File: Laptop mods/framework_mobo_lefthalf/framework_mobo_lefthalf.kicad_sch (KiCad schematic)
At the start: 48 parts, among them J1 USB_C_Receptacle, J2 IF, J5 Display, M1 AltmodeFriend, Q1 BC847, Q2 Q_PMOS_GSD, Q3 BC847, Q4 Q_PMOS_GSD, U1 VL170, U2 FSUSB30MUX, U3 AP1117-33

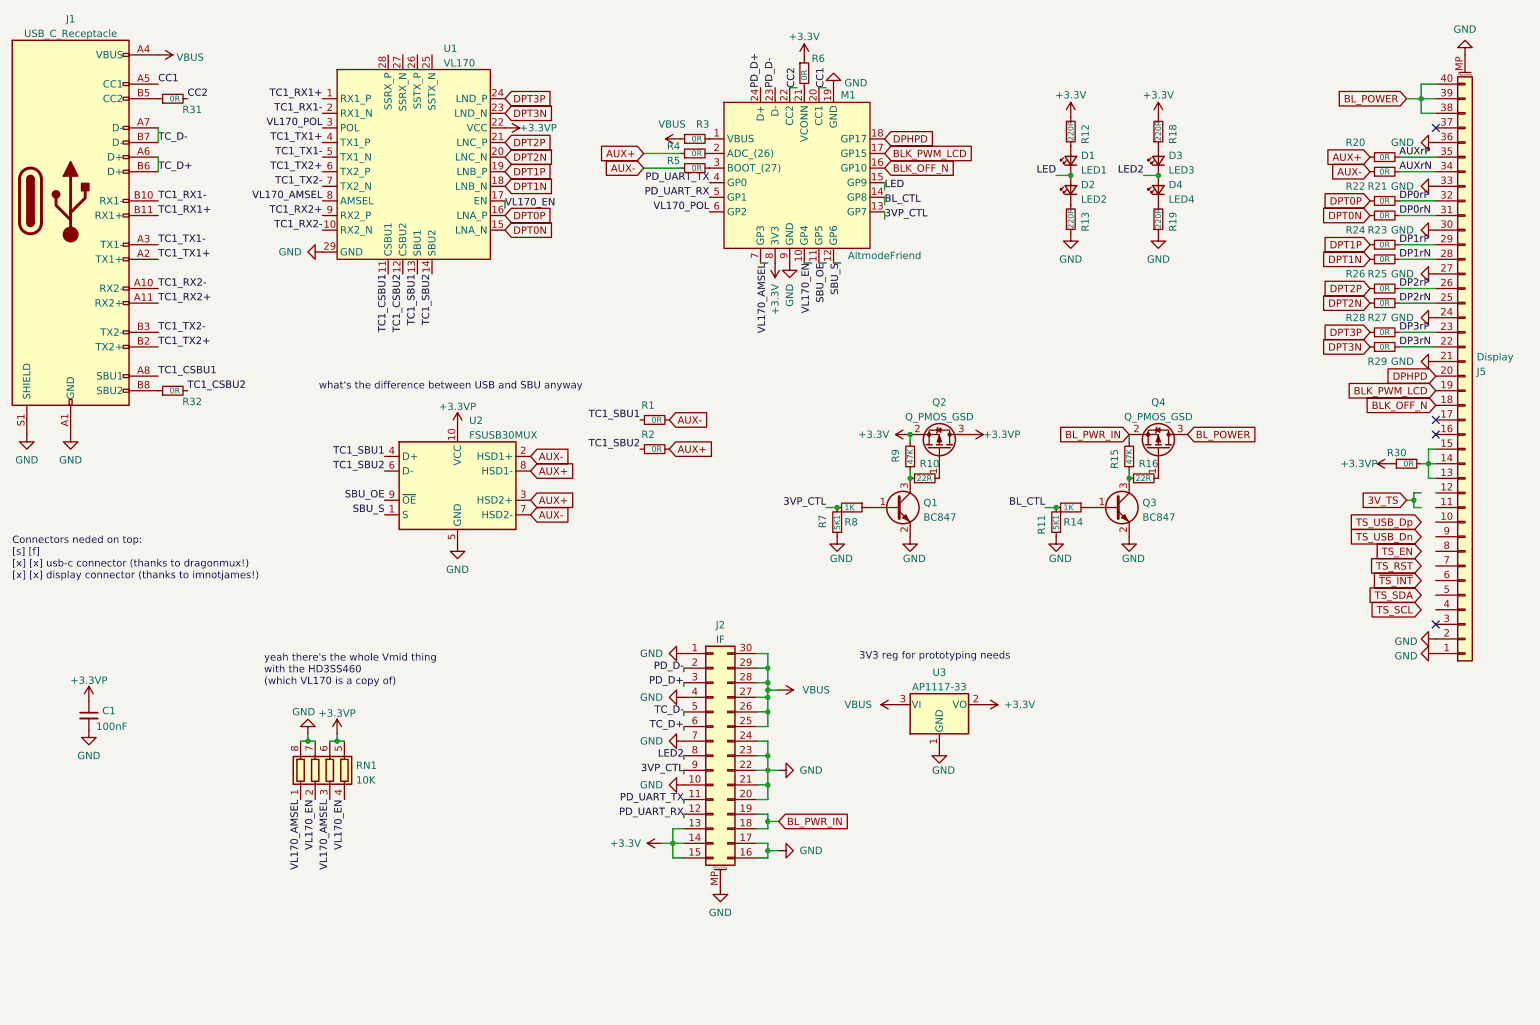
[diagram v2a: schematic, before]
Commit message: framework_mobo_lefthalf: had to rearrange order of DP lanes from the mux, now done
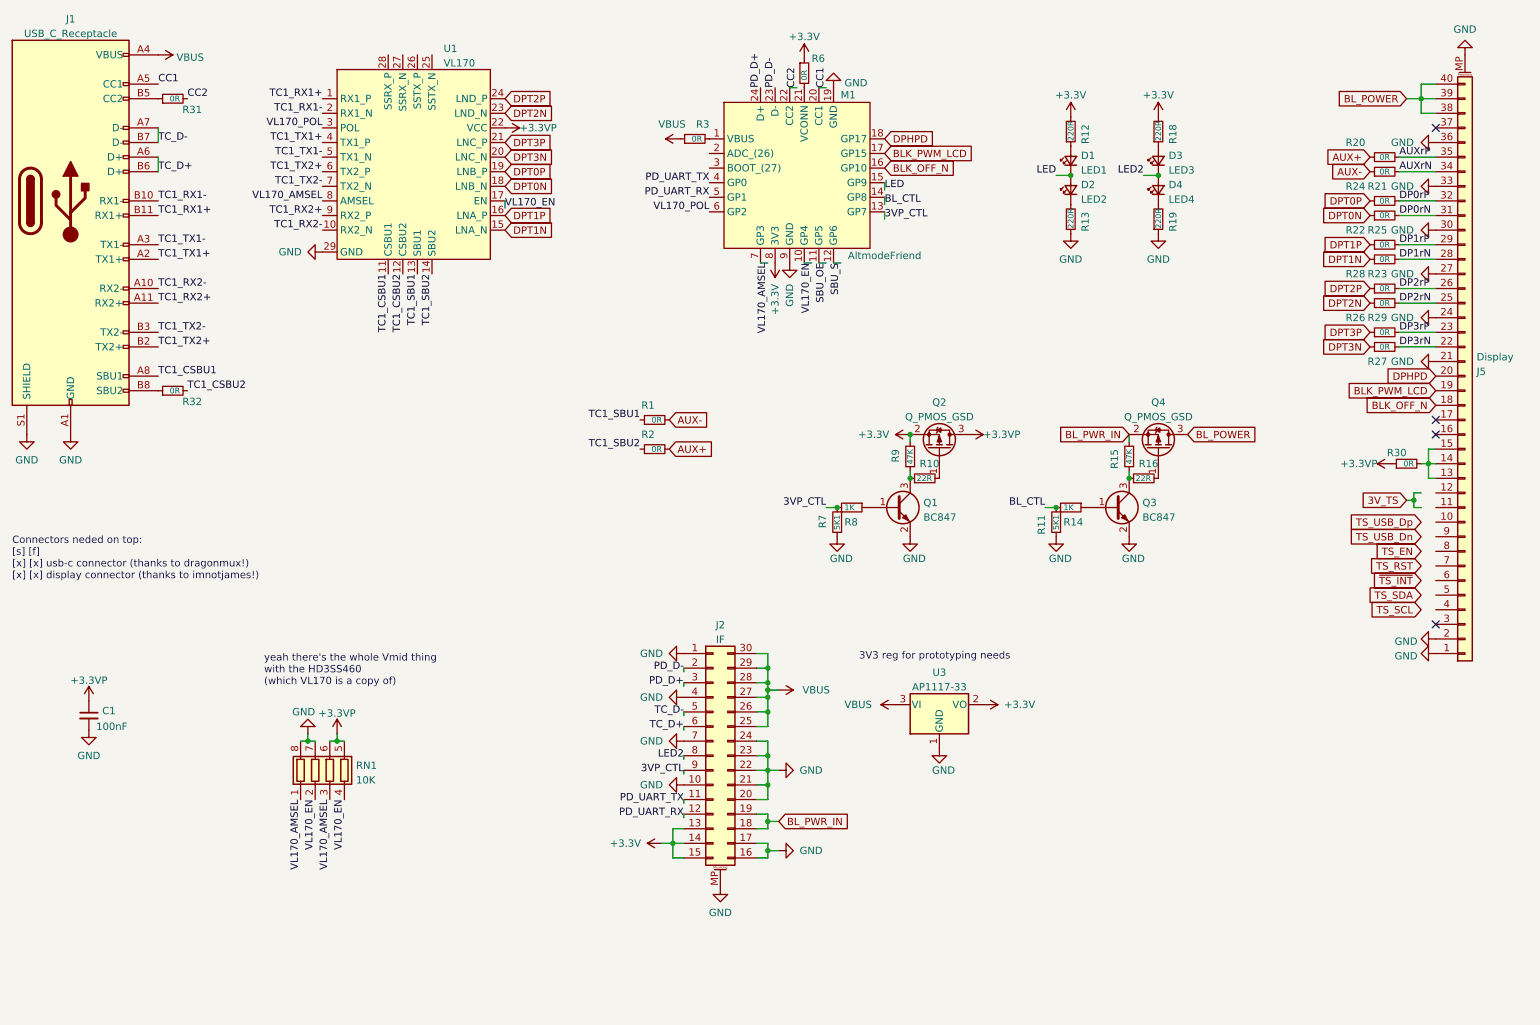
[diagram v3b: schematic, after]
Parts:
- removed R4, R5: 0R, Resistor_SMD:R_0402_1005Metric, symbol Device:R_Small
- removed U2: FSUSB30MUX, Package_SO:MSOP-10_3x3mm_P0.5mm, symbol Interface_USB:FSUSB30MUX
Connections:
- net DP0rN: now also R25.2; no longer R23.2
- net DP0rP: now also R24.2; no longer R22.2
- net DP1rN: now also R23.2; no longer R25.2
- net DP1rP: now also R22.2; no longer R24.2
- net DP2rN: now also R29.2; no longer R27.2
- net DP2rP: now also R28.2; no longer R26.2
- net DP3rN: now also R27.2; no longer R29.2
- net DP3rP: now also R26.2; no longer R28.2
- net DPT0N: now also R25.1, U1.18 (LNB_N); no longer R23.1, U1.15 (LNA_N)
- net DPT0P: now also R24.1, U1.19 (LNB_P); no longer R22.1, U1.16 (LNA_P)
- net DPT1N: now also R23.1, U1.15 (LNA_N); no longer R25.1, U1.18 (LNB_N)
- net DPT1P: now also R22.1, U1.16 (LNA_P); no longer R24.1, U1.19 (LNB_P)
- net DPT2N: now also R29.1, U1.23 (LND_N); no longer R27.1, U1.20 (LNC_N)
- net DPT2P: now also R28.1, U1.24 (LND_P); no longer R26.1, U1.21 (LNC_P)
- net DPT3N: now also R27.1, U1.20 (LNC_N); no longer R29.1, U1.23 (LND_N)
- net DPT3P: now also R26.1, U1.21 (LNC_P); no longer R28.1, U1.24 (LND_P)
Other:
- note removed: "what's the difference between USB and SBU anyway"
- moved on the sheet: R22, R23, R24, R25, R26, R27, R28, R29
